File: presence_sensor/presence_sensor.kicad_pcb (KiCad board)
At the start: 2 copper layers, 50 x 50 mm, 46 parts, among them J1 SG_UL, J10 SWITCH, J2 SG_UR, J3 SG_LL, J30 D_OUT, J31 OPTO, J4 SG_LR, J40 LOAD, J5 FULL_BRIDGE, J50 12V_IN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

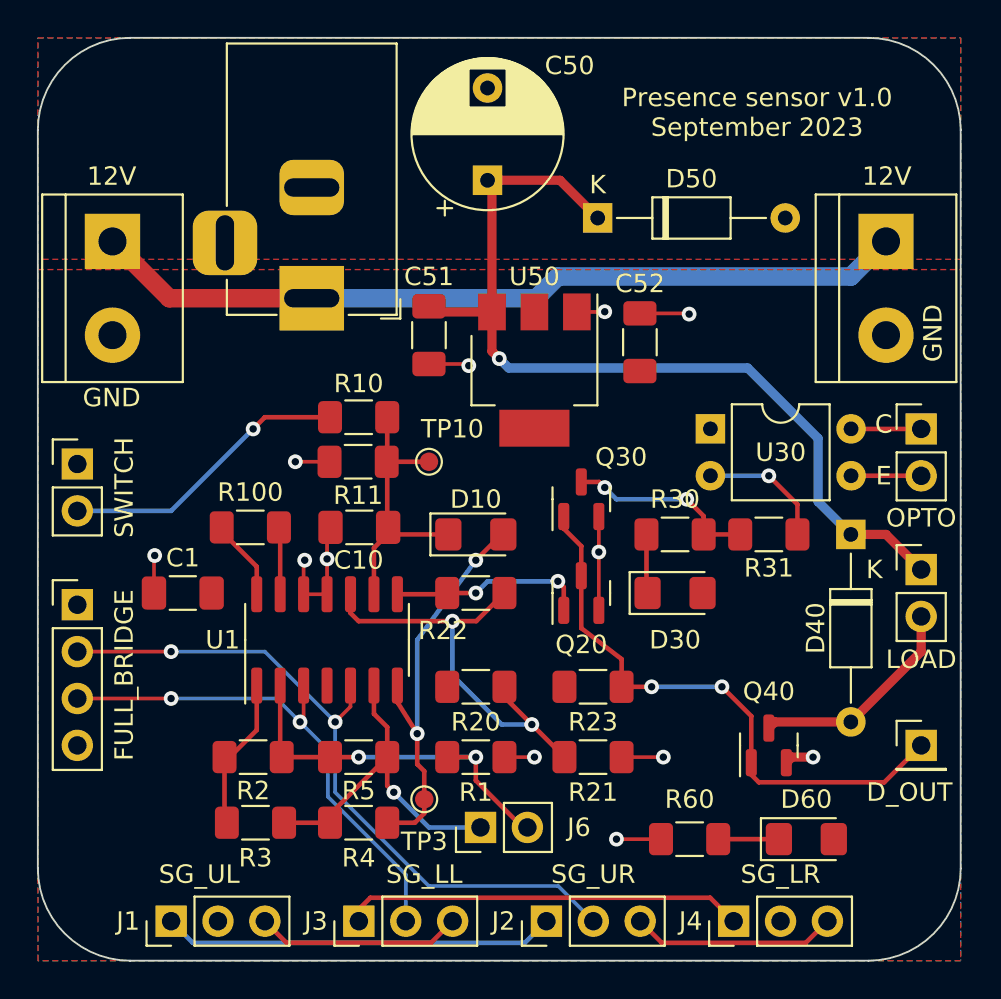
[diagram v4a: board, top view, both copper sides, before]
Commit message: Move presence indicator LED.
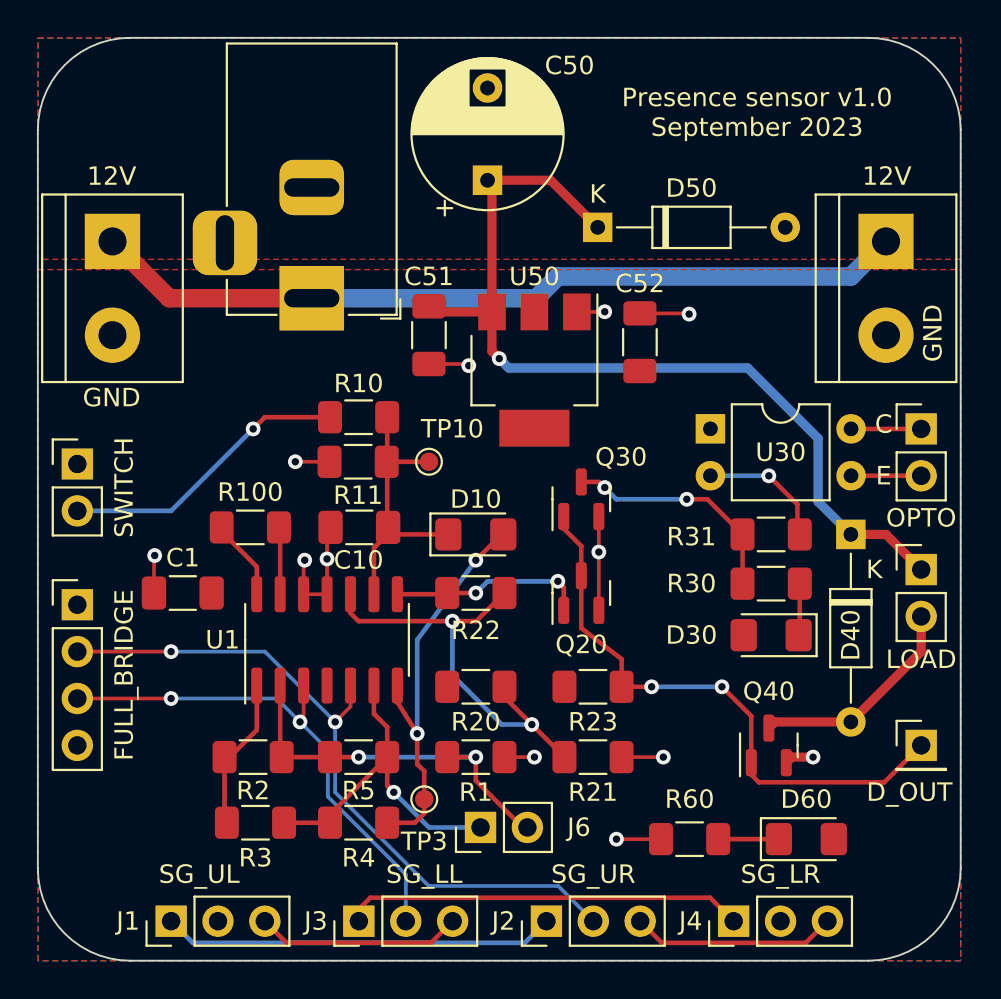
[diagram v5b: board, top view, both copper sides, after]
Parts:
- moved R30 5.85 mm to (89.7, 79.6), turned to 180 degrees
- moved D30 5.69 mm to (89.7, 82.4), turned to 180 degrees
- moved D50 0.51 mm to (80.3, 60.3)
- moved R31 0.13 mm to (89.7, 76.9)
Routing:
- net Net-(Q30-Pad3): track 10.4 -> 12.6 mm
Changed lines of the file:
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@@
   )
   (footprint "Resistor_SMD:R_1206_3216Metric_Pad1.30x1.75mm_HandSolder" (layer "F.Cu")
-    (at 84.525 76.905)
+    (at 89.732 79.572 180)
     (descr "Resistor SMD 1206 (3216 Metric), square (rectangular) end terminal, IPC_7351 nominal with elongated pad for handsoldering. (Body size source: IPC-SM-782 page 72, https://www.pcb-3d.com/wordpress/wp-content/uploads/ipc-sm-782a_amendment_1_and_2.pdf), generated with kicad-footprint-generator")
     (tags "resistor handsolder")
@@
     (property "Sheetname" "")
     (attr smd)
-    (fp_text reference "R30" (at 0 -1.905) (layer "F.SilkS")
+    (fp_text reference "R30" (at 4.318 0) (layer "F.SilkS")
       (effects (font (size 1 1) (thickness 0.15)))
     )
@@
     (fp_line (start -1.6 -0.8) (end 1.6 -0.8) (layer "F.Fab") (width 0.1))
     (fp_line (start 1.6 0.8) (end -1.6 0.8) (layer "F.Fab") (width 0.1))
-    (pad "1" smd roundrect (at -1.55 0) (size 1.3 1.75) (layers "F.Cu" "F.Paste" "F.Mask") (roundrect_rratio 0.192308)
+    (pad "1" smd roundrect (at -1.55 0 180) (size 1.3 1.75) (layers "F.Cu" "F.Paste" "F.Mask") (roundrect_rratio 0.192308)
       (net 6 "Net-(D30-Pad1)") (pintype "passive"))
-    (pad "2" smd roundrect (at 1.55 0) (size 1.3 1.75) (layers "F.Cu" "F.Paste" "F.Mask") (roundrect_rratio 0.192308)
+    (pad "2" smd roundrect (at 1.55 0 180) (size 1.3 1.75) (layers "F.Cu" "F.Paste" "F.Mask") (roundrect_rratio 0.192308)
       (net 20 "Net-(Q30-Pad3)") (pintype "passive"))
     (model "${KICAD6_3DMODEL_DIR}/Resistor_SMD.3dshapes/R_1206_3216Metric.wrl"
@@
   )
   (footprint "Diode_THT:D_DO-35_SOD27_P10.16mm_Horizontal" (layer "F.Cu")
-    (at 80.334 59.76)
+    (at 80.334 60.268)
     (descr "Diode, DO-35_SOD27 series, Axial, Horizontal, pin pitch=10.16mm, , length*diameter=4*2mm^2, , http://www.diodes.com/_files/packages/DO-35.pdf")
     (tags "Diode DO-35_SOD27 series Axial Horizontal pin pitch 10.16mm  length 4mm diameter 2mm")
@@
   )
   (footprint "Resistor_SMD:R_1206_3216Metric_Pad1.30x1.75mm_HandSolder" (layer "F.Cu")
-    (at 89.605 76.905 180)
+    (at 89.732 76.905 180)
     (descr "Resistor SMD 1206 (3216 Metric), square (rectangular) end terminal, IPC_7351 nominal with elongated pad for handsoldering. (Body size source: IPC-SM-782 page 72, https://www.pcb-3d.com/wordpress/wp-content/uploads/ipc-sm-782a_amendment_1_and_2.pdf), generated with kicad-footprint-generator")
     (tags "resistor handsolder")
@@
     (property "Sheetname" "")
     (attr smd)
-    (fp_text reference "R31" (at 0 -1.82) (layer "F.SilkS")
+    (fp_text reference "R31" (at 4.318 -0.127) (layer "F.SilkS")
       (effects (font (size 1 1) (thickness 0.15)))
     )
@@
   )
   (footprint "LED_SMD:LED_1206_3216Metric_Pad1.42x1.75mm_HandSolder" (layer "F.Cu")
-    (at 84.525 80.08)
+    (at 89.732 82.366 180)
     (descr "LED SMD 1206 (3216 Metric), square (rectangular) end terminal, IPC_7351 nominal, (Body size source: http://www.tortai-tech.com/upload/download/2011102023233369053.pdf), generated with kicad-footprint-generator")
     (tags "LED handsolder")
@@
     (property "Sheetname" "")
     (attr smd)
-    (fp_text reference "D30" (at 0 2.54) (layer "F.SilkS")
+    (fp_text reference "D30" (at 4.318 0) (layer "F.SilkS")
       (effects (font (size 1 1) (thickness 0.15)))
     )
@@
     (fp_line (start -1.2 -0.8) (end -1.6 -0.4) (layer "F.Fab") (width 0.1))
     (fp_line (start -1.6 0.8) (end 1.6 0.8) (layer "F.Fab") (width 0.1))
-    (pad "1" smd roundrect (at -1.4875 0) (size 1.425 1.75) (layers "F.Cu" "F.Paste" "F.Mask") (roundrect_rratio 0.175439)
+    (pad "1" smd roundrect (at -1.4875 0 180) (size 1.425 1.75) (layers "F.Cu" "F.Paste" "F.Mask") (roundrect_rratio 0.175439)
       (net 6 "Net-(D30-Pad1)") (pinfunction "K") (pintype "passive"))
-    (pad "2" smd roundrect (at 1.4875 0) (size 1.425 1.75) (layers "F.Cu" "F.Paste" "F.Mask") (roundrect_rratio 0.175439)
+    (pad "2" smd roundrect (at 1.4875 0 180) (size 1.425 1.75) (layers "F.Cu" "F.Paste" "F.Mask") (roundrect_rratio 0.175439)
       (net 1 "E+") (pinfunction "A") (pintype "passive"))
     (model "${KICAD6_3DMODEL_DIR}/LED_SMD.3dshapes/LED_1206_3216Metric.wrl"
@@
     (property "Sheetname" "")
     (attr through_hole)
-    (fp_text reference "D40" (at 5.08 1.905 -90) (layer "F.SilkS")
+    (fp_text reference "D40" (at 5.461 0 -90) (layer "F.SilkS")
       (effects (font (size 1 1) (thickness 0.15)))
     )
@@
     (property "Sheetname" "")
     (attr smd)
-    (fp_text reference "R22" (at 1.778 -2.032) (layer "F.SilkS")
+    (fp_text reference "R22" (at 0 -2.032) (layer "F.SilkS")
       (effects (font (size 1 1) (thickness 0.15)))
     )
@@
   (segment (start 79.205 64.85) (end 80.705 64.85) (width 0.2) (layer "F.Cu") (net 2))
   (segment (start 80.395 77.86) (end 80.395 81.0175) (width 0.2) (layer "F.Cu") (net 2))
-  (segment (start 82.62 64.9285) (end 82.5315 64.84) (width 0.2) (layer "F.Cu") (net 2))
   (segment (start 76.905 88.97) (end 75.28 88.97) (width 0.2) (layer "F.Cu") (net 2))
   (segment (start 65.804 72.968) (end 63.951 72.968) (width 0.2) (layer "F.Cu") (net 2))
   (segment (start 90.8575 88.97) (end 92 88.97) (width 0.5) (layer "F.Cu") (net 2))
   (segment (start 64.4 80.145) (end 64.4 78.361) (width 0.2) (layer "F.Cu") (net 2))
-  (segment (start 65.8175 73.7425) (end 65.83 73.73) (width 0.2) (layer "F.Cu") (net 2))
   (segment (start 82.62 64.9285) (end 85.2485 64.9285) (width 0.2) (layer "F.Cu") (net 2))
   (segment (start 80.705 64.85) (end 80.715 64.84) (width 0.2) (layer "F.Cu") (net 2))
@@
   (segment (start 68.93 73.73) (end 68.93 76.8925) (width 0.25) (layer "F.Cu") (net 3))
   (segment (start 75 67.38) (end 74.605 66.985) (width 0.5) (layer "F.Cu") (net 4))
-  (segment (start 74.365 57.717651) (end 78.291651 57.717651) (width 0.5) (layer "F.Cu") (net 4))
+  (segment (start 77.783651 57.717651) (end 80.334 60.268) (width 0.5) (layer "F.Cu") (net 4))
   (segment (start 74.605 64.85) (end 71.4925 64.85) (width 0.5) (layer "F.Cu") (net 4))
   (segment (start 74.605 66.985) (end 74.605 64.85) (width 0.5) (layer "F.Cu") (net 4))
-  (segment (start 78.291651 57.717651) (end 80.334 59.76) (width 0.5) (layer "F.Cu") (net 4))
+  (segment (start 74.365 57.717651) (end 77.783651 57.717651) (width 0.5) (layer "F.Cu") (net 4))
   (segment (start 71.4925 64.85) (end 71.19 64.5475) (width 0.5) (layer "F.Cu") (net 4))
   (segment (start 94.05 76.905) (end 95.955 76.905) (width 0.5) (layer "F.Cu") (net 4))
@@
   (segment (start 70.555 87.7) (end 70.555 82.62) (width 0.25) (layer "B.Cu") (net 5))
   (segment (start 70.555 82.62) (end 73.73 78.302) (width 0.25) (layer "B.Cu") (net 5))
-  (segment (start 82.975 80.0175) (end 83.0375 80.08) (width 0.25) (layer "F.Cu") (net 6))
-  (segment (start 82.975 76.905) (end 82.975 80.0175) (width 0.25) (layer "F.Cu") (net 6))
+  (segment (start 91.282 79.572) (end 91.282 82.3035) (width 0.25) (layer "F.Cu") (net 6))
+  (segment (start 91.282 82.3035) (end 91.2195 82.366) (width 0.25) (layer "F.Cu") (net 6))
   (segment (start 89.9375 87.065) (end 94.05 87.065) (width 0.5) (layer "F.Cu") (net 7))
   (segment (start 97.86 83.255) (end 94.05 87.065) (width 0.5) (layer "F.Cu") (net 7))
@@
   (segment (start 73.73 80.08) (end 74.365 79.445) (width 0.25) (layer "B.Cu") (net 19))
   (segment (start 74.365 79.445) (end 78.175 79.445) (width 0.25) (layer "B.Cu") (net 19))
-  (segment (start 86.075 75.915) (end 86.075 76.905) (width 0.25) (layer "F.Cu") (net 20))
   (segment (start 80.4125 74.0625) (end 80.715 74.365) (width 0.25) (layer "F.Cu") (net 20))
   (segment (start 79.445 74.0625) (end 80.4125 74.0625) (width 0.25) (layer "F.Cu") (net 20))
-  (segment (start 85.16 75) (end 86.075 75.915) (width 0.25) (layer "F.Cu") (net 20))
-  (segment (start 86.075 76.905) (end 88.055 76.905) (width 0.25) (layer "F.Cu") (net 20))
+  (segment (start 86.277 75) (end 88.182 76.905) (width 0.25) (layer "F.Cu") (net 20))
+  (segment (start 88.182 76.905) (end 88.182 79.572) (width 0.25) (layer "F.Cu") (net 20))
+  (segment (start 85.16 75) (end 86.277 75) (width 0.25) (layer "F.Cu") (net 20))
   (via (at 85.16 75) (size 0.8) (drill 0.4) (layers "F.Cu" "B.Cu") (net 20))
   (via (at 80.715 74.365) (size 0.8) (drill 0.4) (layers "F.Cu" "B.Cu") (net 20))

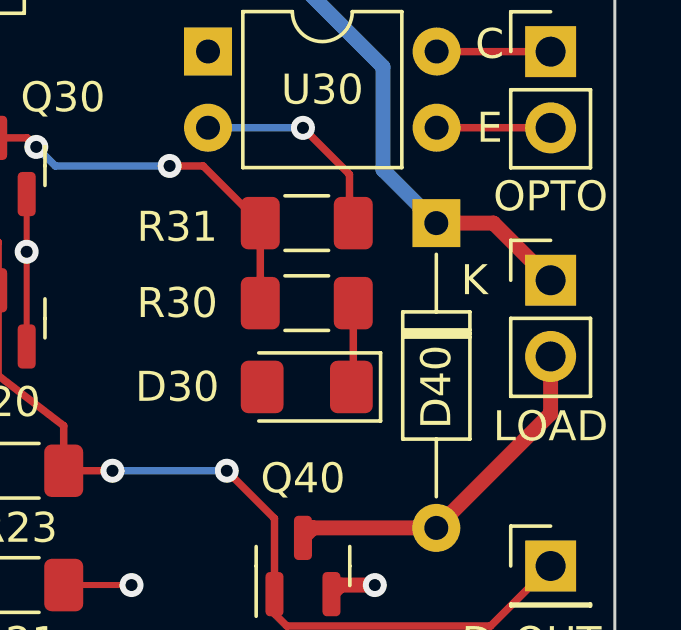
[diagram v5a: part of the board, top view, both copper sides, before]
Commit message: Move presence indicator LED.
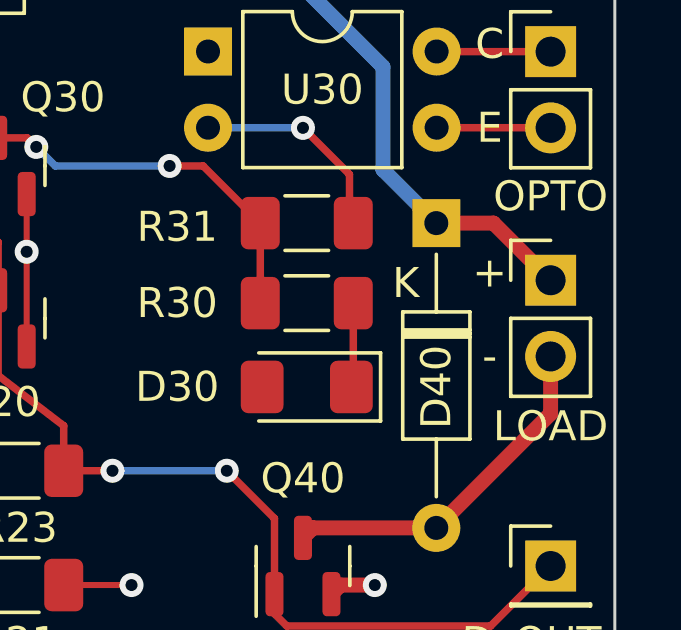
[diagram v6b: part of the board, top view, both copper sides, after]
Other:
- board text added: "+"
- board text added: "-"
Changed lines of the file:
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@@
       (effects (font (size 1 1) (thickness 0.15)))
     )
-    (fp_text user "K" (at 1.905 -1.27) (layer "F.SilkS")
+    (fp_text user "K" (at 2 1.016) (layer "F.SilkS")
       (effects (font (size 1 1) (thickness 0.15)))
     )
@@
     (effects (font (size 1 1) (thickness 0.15)))
   )
+  (gr_text "+" (at 95.828 78.556) (layer "F.SilkS")
+    (effects (font (size 1 1) (thickness 0.15)))
+  )
   (gr_text "GND" (at 98.5 66 90) (layer "F.SilkS")
     (effects (font (size 1 1) (thickness 0.15)))
@@
     (effects (font (size 1 1) (thickness 0.15)))
   )
+  (gr_text "-" (at 95.828 81.35) (layer "F.SilkS")
+    (effects (font (size 1 1) (thickness 0.15)))
+  )

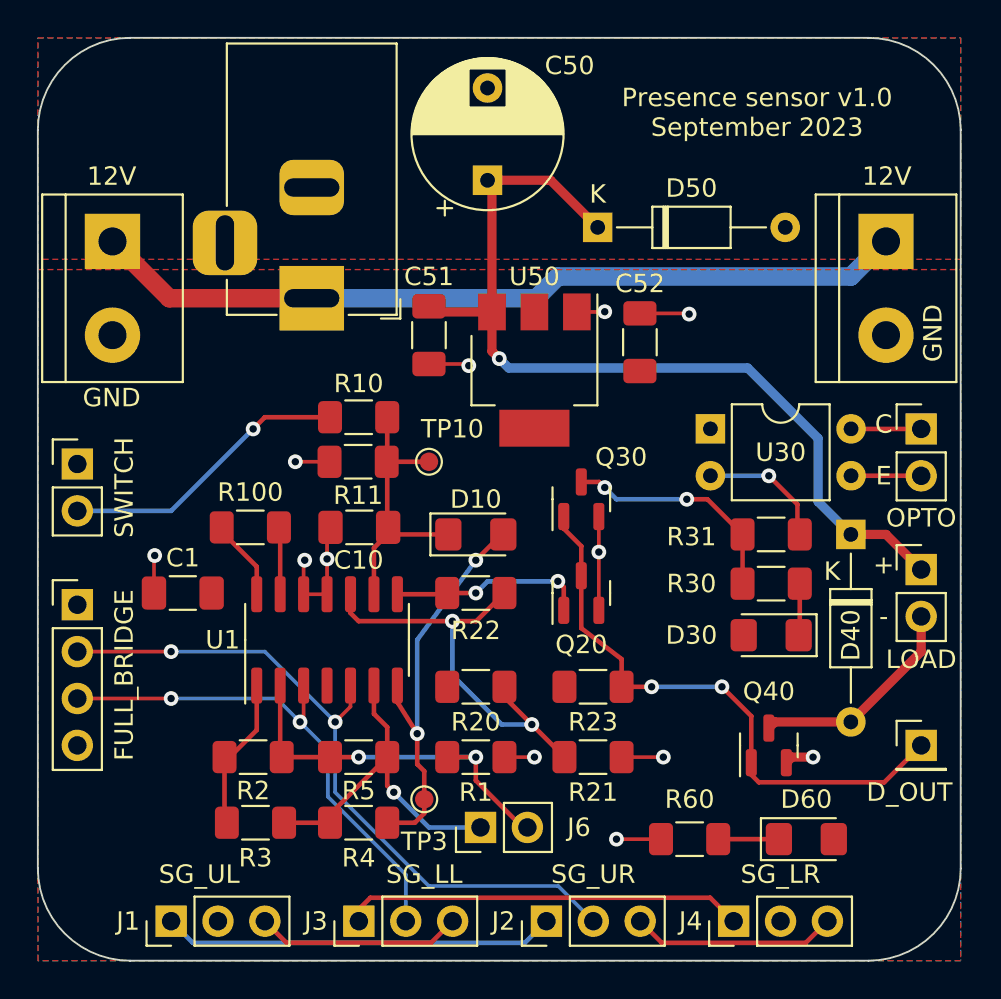
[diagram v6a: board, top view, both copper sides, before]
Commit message: Add mounting holes
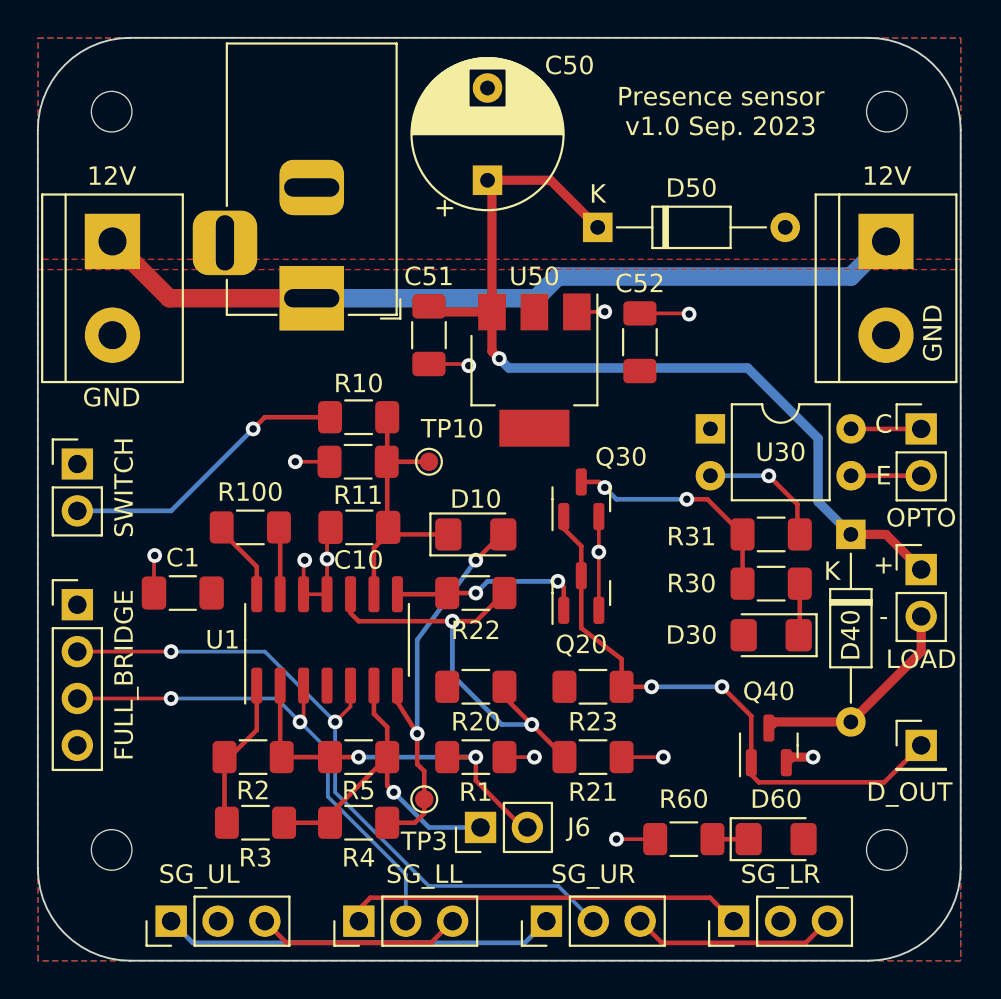
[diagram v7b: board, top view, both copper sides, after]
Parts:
- added REF**: MountingHole_2.2mm_M2, MountingHole:MountingHole_2.2mm_M2, F.Cu at (96.0, 94.0)
- added REF**: MountingHole_2.2mm_M2, MountingHole:MountingHole_2.2mm_M2, F.Cu at (54.0, 94.0)
- added REF**: MountingHole_2.2mm_M2, MountingHole:MountingHole_2.2mm_M2, F.Cu at (54.0, 54.0)
- added REF**: MountingHole_2.2mm_M2, MountingHole:MountingHole_2.2mm_M2, F.Cu at (96.0, 54.0)
- moved D60 1.64 mm to (90.0, 93.4)
- moved R60 0.31 mm to (85.0, 93.4)
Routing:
- net Net-(D60-Pad1): track 3.29 -> 1.96 mm
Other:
- board text added: "Presence sensor v1.0 Sep. 2023"
- board text removed: "Presence sensor v1.0 September 2023"
